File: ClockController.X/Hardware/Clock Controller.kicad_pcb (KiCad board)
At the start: 2 copper layers, 63.5 x 44.5 mm, 48 parts, among them J1 UJC-VP-3-SMT-TR, J2 HDR-1X2H, Q1 DMG7430LFG-7, Q2 FDD7N25LZTM, Q3 MMBT2222A-TP, Q4 MMBT2907ALT1G, Q5 MMBT2222A-TP, Q6 MMBT2222A-TP, U1 PIC16F15224-I/SL, U2 AS78L05RTR-E1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

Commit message: More zones
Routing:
- net +5V: track 51.1 -> 43.0 mm
- added copper zone on B.Cu, net +5V
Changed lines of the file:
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@@
-	)
-	(segment
-		(start 141.985965 119.379965)
-		(end 136.332 119.379965)
-		(width 1.27)
-		(layer "B.Cu")
-		(net 2)
-	)
-	(segment
-		(start 142.24 119.38)
-		(end 141.986 119.38)
-		(width 0.2)
-		(layer "B.Cu")
-		(net 2)
-	)
-	(segment
-		(start 136.332 121.5385)
-		(end 136.27 121.6005)
-		(width 1.27)
-		(layer "B.Cu")
-		(net 2)
-	)
-	(segment
-		(start 136.332 119.379965)
-		(end 136.332 121.5385)
-		(width 1.27)
-		(layer "B.Cu")
-		(net 2)
-	)
-	(segment
-		(start 141.986 119.38)
-		(end 141.985965 119.379965)
-		(width 0.2)
-		(layer "B.Cu")
-		(net 2)
 	)
 	(segment
@@
 	)
 	(zone
+		(net 2)
+		(net_name "+5V")
+		(layer "B.Cu")
+		(hatch edge 0.5)
+		(priority 10)
+		(connect_pads yes
+			(clearance 0.5)
+		)
+		(min_thickness 0.25)
+		(filled_areas_thickness no)
+		(fill yes
+			(thermal_gap 0.5)
+			(thermal_bridge_width 0.5)
+			(smoothing fillet)
+			(radius 0.254)
+		)
+		(polygon
+			(pts
+				(xy 135.89 118.618) (xy 142.494 118.618) (xy 142.494 120.142) (xy 136.906 122.174) (xy 135.636 122.174)
+				(xy 135.636 121.158)
+			)
+		)
+	)
+	(zone

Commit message: Small layout adjustments
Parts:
- moved PWM0 2.30 mm to (141.2, 111.5)
- moved C4 1.65 mm to (166.6, 122.4), turned to 90.0029 degrees
- moved C2 1.50 mm to (134.3, 110.7)
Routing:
- net GND: track 22.7 -> 20.2 mm
- net V5V: track 100.7 -> 98.6 mm

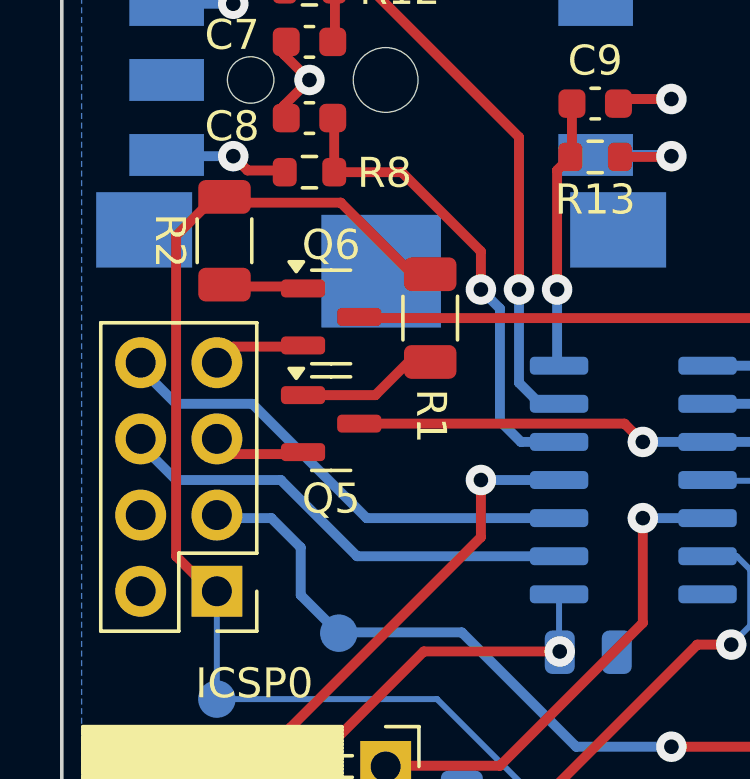
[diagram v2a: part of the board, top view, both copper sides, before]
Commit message: Simplified I2C cutoff
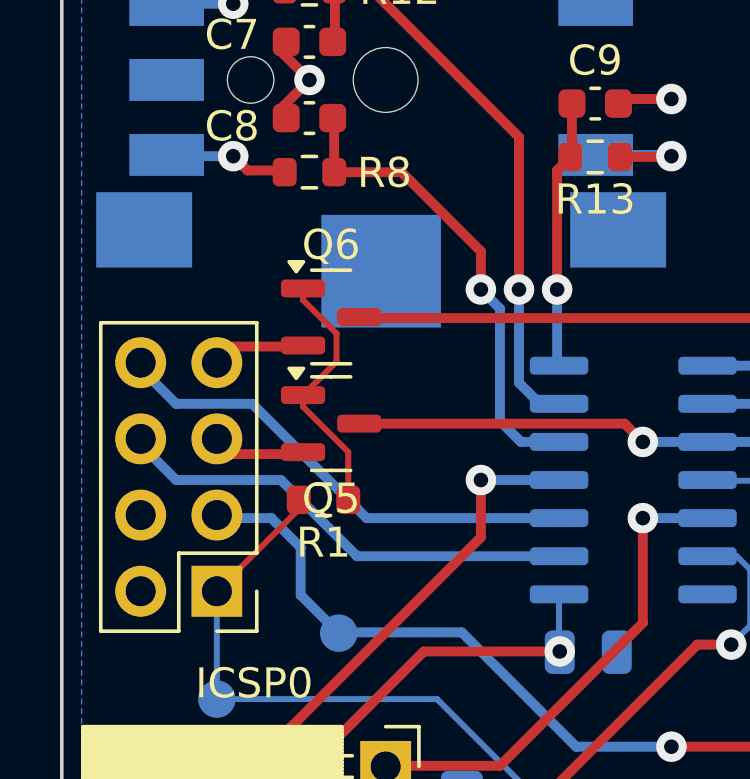
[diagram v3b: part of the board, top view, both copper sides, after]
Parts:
- removed R2: 2.2k, Resistor_SMD:R_1206_3216Metric
- R1: footprint Resistor_SMD:R_1206_3216Metric -> Resistor_SMD:R_0603_1608Metric
- moved R1 7.02 mm to (125.5, 105.7), turned to -179.999 degrees
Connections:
- Q6 pad 1: Net-(Q6-B) -> Net-(Q5-B)
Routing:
- net +5V: track 43.0 -> 25.1 mm
- net Net-(Q5-B): track 4.19 -> 8.60 mm
- net Net-(Q6-B): track 2.67 -> 0.00 mm

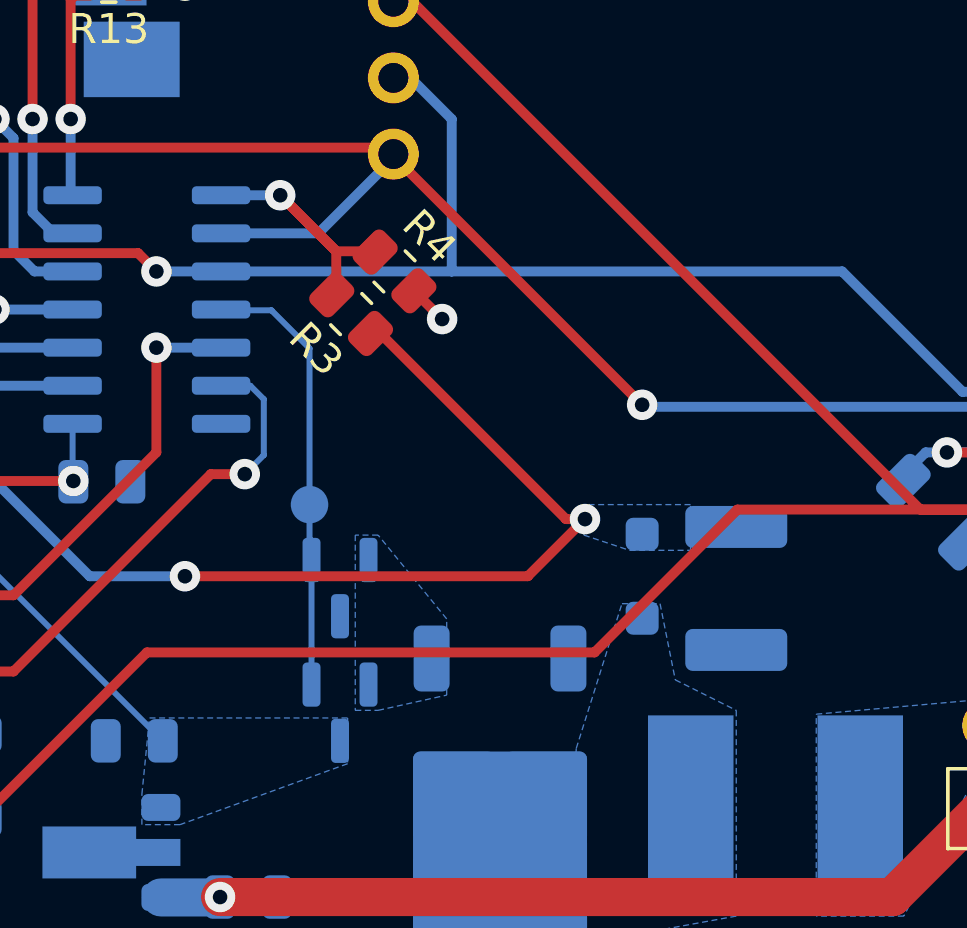
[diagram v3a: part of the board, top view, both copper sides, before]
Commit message: Moved C3
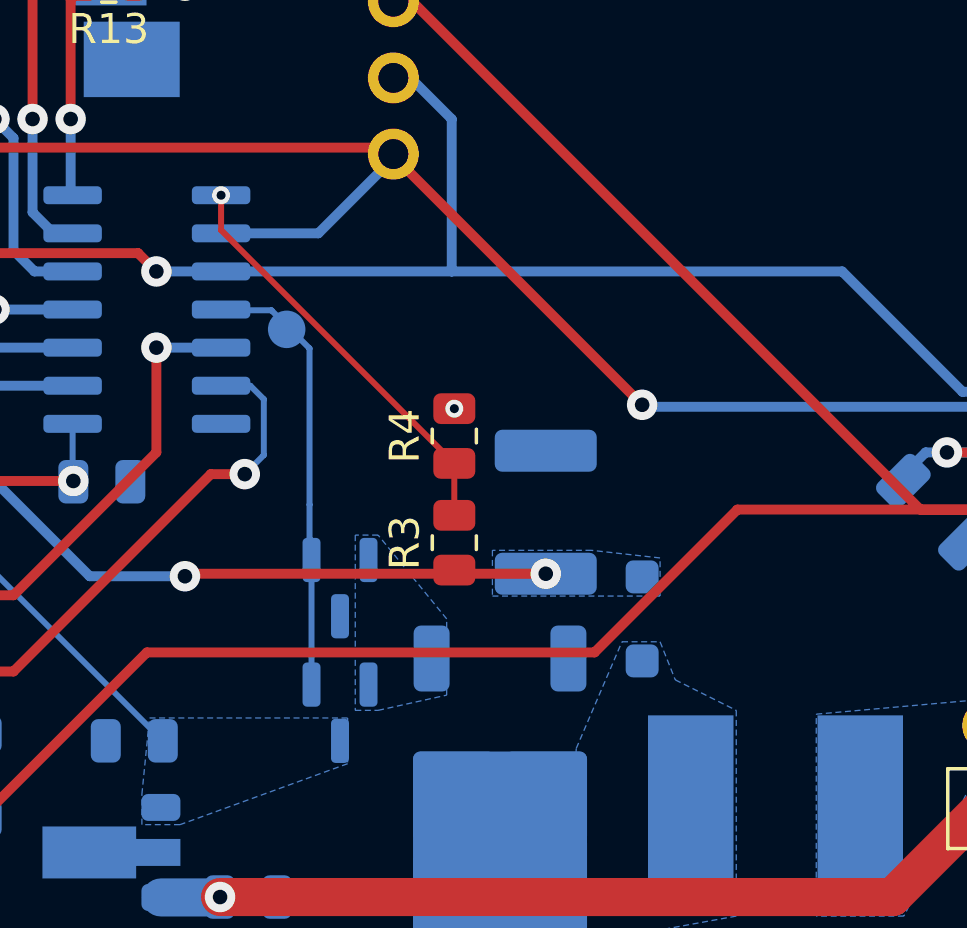
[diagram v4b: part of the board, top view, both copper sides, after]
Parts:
- moved R3 8.36 mm to (146.1, 112.8), turned to 90 degrees
- moved C3 6.84 mm to (149.1, 111.8), turned to -89.9952 degrees
- moved PWM0 5.89 mm to (140.5, 105.7)
- moved R4 5.84 mm to (146.1, 109.2), turned to 90 degrees
- moved D1 1.42 mm to (152.3, 115.3)
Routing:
- net VNN: track 43.0 -> 31.4 mm
- net HV_Mon: track 9.85 -> 13.9 mm
- net GND: track 20.2 -> 18.9 mm
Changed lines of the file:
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@@
 	(footprint "Resistor_SMD:R_0805_2012Metric"
 		(layer "F.Cu")
-		(at 142.610765 105.156 135)
+		(at 146.05 112.776 90)
 		(descr "Resistor SMD 0805 (2012 Metric), square (rectangular) end terminal, IPC_7351 nominal, (Body size source: IPC-SM-782 page 72, https://www.pcb-3d.com/wordpress/wp-content/uploads/ipc-sm-782a_amendment_1_and_2.pdf), generated with kicad-footprint-generator")
 		(tags "resistor")
 		(property "Reference" "R3"
-			(at 0 -1.65 135)
+			(at 0 -1.65 90)
 			(layer "F.SilkS")
 			(effects
@@
 		)
 		(property "Value" "750k"
-			(at 0 1.65 135)
+			(at 0 1.65 90)
 			(layer "F.Fab")
 			(effects
@@
 		)
 		(property "Datasheet" ""
-			(at 0 0 135)
+			(at 0 0 90)
 			(unlocked yes)
 			(layer "F.Fab")
@@
 		)
 		(property "Description" ""
-			(at 0 0 135)
+			(at 0 0 90)
 			(unlocked yes)
 			(layer "F.Fab")
@@
 		)
 		(fp_line
-			(start 1.68 0.95)
-			(end -1.68 0.95)
+			(start -1.68 -0.95)
+			(end 1.68 -0.95)
 			(stroke
 				(width 0.05)
@@
 		)
 		(fp_line
-			(start -1.68 -0.95)
-			(end 1.68 -0.95)
+			(start 1.68 0.95)
+			(end -1.68 0.95)
 			(stroke
 				(width 0.05)
@@
 		)
 		(fp_line
-			(start 1 0.625)
-			(end -1 0.625)
+			(start -1 -0.625)
+			(end 1 -0.625)
 			(stroke
 				(width 0.1)
@@
 		)
 		(fp_line
-			(start -1 -0.625)
-			(end 1 -0.625)
+			(start 1 0.625)
+			(end -1 0.625)
 			(stroke
 				(width 0.1)
@@
 		)
 		(fp_text user "${REFERENCE}"
-			(at 0 0 135)
+			(at 0 0 90)
 			(layer "F.Fab")
 			(effects
@@
 		)
 		(pad "1" smd roundrect
-			(at -0.9125 0 135)
+			(at -0.9125 0 90)
 			(size 1.025 1.4)
 			(layers "F.Cu" "F.Mask" "F.Paste")
@@
 		)
 		(pad "2" smd roundrect
-			(at 0.9125 0 135)
+			(at 0.9125 0 90)
 			(size 1.025 1.4)
 			(layers "F.Cu" "F.Mask" "F.Paste")
@@
 	(footprint "Resistor_SMD:R_0805_2012Metric"
 		(layer "F.Cu")
-		(at 144.0561 103.7336 -45)
+		(at 146.05 109.22 90)
 		(descr "Resistor SMD 0805 (2012 Metric), square (rectangular) end terminal, IPC_7351 nominal, (Body size source: IPC-SM-782 page 72, https://www.pcb-3d.com/wordpress/wp-content/uploads/ipc-sm-782a_amendment_1_and_2.pdf), generated with kicad-footprint-generator")
 		(tags "resistor")
 		(property "Reference" "R4"
-			(at 0 -1.65 315)
+			(at 0 -1.65 90)
 			(layer "F.SilkS")
 			(effects
@@
 		)
 		(property "Value" "12k"
-			(at 0 1.65 315)
+			(at 0 1.65 90)
 			(layer "F.Fab")
 			(effects
@@
 		)
 		(property "Datasheet" ""
-			(at 0 0 315)
+			(at 0 0 90)
 			(unlocked yes)
 			(layer "F.Fab")
@@
 		)
 		(property "Description" ""
-			(at 0 0 315)
+			(at 0 0 90)
 			(unlocked yes)
 			(layer "F.Fab")
@@
 		(attr smd)
 		(fp_line
-			(start -0.227064 0.735)
-			(end 0.227064 0.735)
+			(start -0.227064 -0.735)
+			(end 0.227064 -0.735)
 			(stroke
 				(width 0.12)
@@
 		)
 		(fp_line
-			(start -0.227064 -0.735)
-			(end 0.227064 -0.735)
+			(start -0.227064 0.735)
+			(end 0.227064 0.735)
 			(stroke
 				(width 0.12)
@@
 		)
 		(fp_line
-			(start -1.68 0.95)
-			(end -1.68 -0.95)
+			(start 1.68 -0.95)
+			(end 1.68 0.95)
 			(stroke
 				(width 0.05)
@@
 		)
 		(fp_line
-			(start 1.68 -0.95)
-			(end 1.68 0.95)
+			(start -1.68 0.95)
+			(end -1.68 -0.95)
 			(stroke
 				(width 0.05)
@@
 		)
 		(fp_line
-			(start -1 0.625)
-			(end -1 -0.625)
+			(start 1 -0.625)
+			(end 1 0.625)
 			(stroke
 				(width 0.1)
@@
 		)
 		(fp_line
-			(start 1 -0.625)
-			(end 1 0.625)
+			(start -1 0.625)
+			(end -1 -0.625)
 			(stroke
 				(width 0.1)
@@
 		)
 		(fp_text user "${REFERENCE}"
-			(at 0 0 315)
+			(at 0 0 90)
 			(layer "F.Fab")
 			(effects
@@
 		)
 		(pad "1" smd roundrect
-			(at -0.9125 0 315)
+			(at -0.9125 0 90)
 			(size 1.025 1.4)
 			(layers "F.Cu" "F.Mask" "F.Paste")
@@
 		)
 		(pad "2" smd roundrect
-			(at 0.9125 0 315)
+			(at 0.9125 0 90)
 			(size 1.025 1.4)
 			(layers "F.Cu" "F.Mask" "F.Paste")
@@
 	(footprint "Diode_SMD:D_SOD-123F"
 		(layer "B.Cu")
-		(at 152.311111 113.8936 -89.99726403)
+		(at 152.311111 115.316 -89.99726403)
 		(descr "D_SOD-123F")
 		(tags "D_SOD-123F")
 		(property "Reference" "D1"
-			(at -0.127 1.905 90.00273597)
+			(at 0.000089 -1.866889 90.00273597)
 			(layer "B.SilkS")
 			(effects
@@
 	(footprint "Clock Controller:TP_1.25MM"
 		(layer "B.Cu")
-		(at 141.224 111.506 90.002)
+		(at 140.462 105.664 90.002)
 		(property "Reference" "PWM0"
 			(at 0 0 90.002)
@@
 	(footprint "Capacitor_SMD:C_1812_4532Metric"
 		(layer "B.Cu")
-		(at 155.448 114.3 90.00484056)
+		(at 149.098 111.76 -89.99515944)
 		(descr "Capacitor SMD 1812 (4532 Metric), square (rectangular) end terminal, IPC-7351 nominal, (Body size source: IPC-SM-782 page 76, https://www.pcb-3d.com/wordpress/wp-content/uploads/ipc-sm-782a_amendment_1_and_2.pdf), generated with kicad-footprint-generator")
 		(tags "capacitor")
 		(property "Reference" "C3"
-			(at 0 2.65 270.0048406)
+			(at -3.81 -0.000322 180.0048406)
 			(layer "B.SilkS")
 			(effects
@@
 		)
 		(property "Value" "10uF"
-			(at 0 -2.65 270.0048406)
+			(at 0 -2.65 90.0048406)
 			(layer "B.Fab")
 			(effects
@@
 		)
 		(property "Datasheet" ""
-			(at 0 0 270.0048406)
+			(at 0 0 90.0048406)
 			(layer "B.Fab")
 			(hide yes)
@@
 		)
 		(property "Description" ""
-			(at 0 0 270.0048406)
+			(at 0 0 90.0048406)
 			(layer "B.Fab")
 			(hide yes)
@@
 		(attr smd)
 		(fp_line
-			(start -1.161252 -1.71)
-			(end 1.161252 -1.71)
+			(start -1.161252 1.71)
+			(end 1.161252 1.71)
 			(stroke
 				(width 0.12)
@@
 		)
 		(fp_line
-			(start -1.161252 1.71)
-			(end 1.161252 1.71)
+			(start -1.161252 -1.71)
+			(end 1.161252 -1.71)
 			(stroke
 				(width 0.12)
@@
 		)
 		(fp_text user "${REFERENCE}"
-			(at 0 0 270.0048406)
+			(at 0 0 90.0048406)
 			(layer "B.Fab")
 			(effects
@@
 		)
 		(pad "1" smd roundrect
-			(at -2.05 0 90.00484056)
+			(at -2.05 0 270.0048406)
 			(size 1.4 3.4)
 			(layers "B.Cu" "B.Mask" "B.Paste")
@@
 		)
 		(pad "2" smd roundrect
-			(at 2.05 0 90.00484056)
+			(at 2.05 0 270.0048406)
 			(size 1.4 3.4)
 			(layers "B.Cu" "B.Mask" "B.Paste")
@@
 	)
 	(gr_text "PWM"
-		(at 146.558 112.268 359.9976849)
+		(at 145.796 106.426 359.9976849)
 		(layer "B.SilkS")
 		(effects
@@
 	)
 	(segment
-		(start 144.727867 104.405367)
-		(end 144.727867 104.405367)
-		(width 0.33)
-		(layer "F.Cu")
-		(net 8)
-	)
-	(segment
 		(start 124.1561 92.938633)
 		(end 124.1561 92.5186)
@@
 	)
 	(segment
-		(start 145.6436 105.3211)
-		(end 144.727867 104.405367)
-		(width 0.33)
-		(layer "F.Cu")
-		(net 8)
-	)
-	(segment
 		(start 124.1561 92.5186)
 		(end 125.0061 91.6686)
@@
 	)
 	(via
-		(at 165.6461 105.3211)
-		(size 1.016)
-		(drill 0.485667)
+		(at 146.05 108.3075)
+		(size 0.6)
+		(drill 0.3)
 		(layers "F.Cu" "B.Cu")
 		(net 8)
 	)
 	(via
-		(at 145.6436 105.3211)
+		(at 165.6461 105.3211)
 		(size 1.016)
 		(drill 0.485667)
@@
 	)
 	(segment
-		(start 140.2461 101.1936)
-		(end 142.114333 103.061833)
-		(width 0.33)
-		(layer "F.Cu")
-		(net 9)
-	)
-	(segment
-		(start 140.2461 101.1936)
-		(end 142.114333 103.061833)
-		(width 0.33)
+		(start 146.05 111.8635)
+		(end 146.05 110.1325)
+		(width 0.2)
 		(layer "F.Cu")
 		(net 9)
 	)
 	(segment
-		(start 142.114333 103.061833)
-		(end 142.114333 104.331833)
-		(width 0.33)
+		(start 138.2761 102.3586)
+		(end 138.2761 101.1936)
+		(width 0.2)
 		(layer "F.Cu")
 		(net 9)
 	)
 	(segment
-		(start 142.114333 103.061833)
-		(end 143.384333 103.061833)
-		(width 0.33)
+		(start 146.05 110.1325)
+		(end 138.2761 102.3586)
+		(width 0.2)
 		(layer "F.Cu")
 		(net 9)
 	)
 	(via
-		(at 140.2461 101.1936)
-		(size 1.016)
-		(drill 0.485667)
+		(at 138.2761 101.1936)
+		(size 0.6)
+		(drill 0.3)
 		(layers "F.Cu" "B.Cu")
 		(net 9)
 	)
 	(segment
-		(start 140.2461 101.1936)
-		(end 140.2461 101.1936)
-		(width 0.33)
-		(layer "B.Cu")
-		(net 9)
-	)
-	(segment
-		(start 138.2211 101.1936)
-		(end 140.2461 101.1936)
-		(width 0.33)
-		(layer "B.Cu")
-		(net 9)
-	)
-	(segment
 		(start 163.7561 104.1636)
 		(end 164.1861 103.7336)
@@
 	)
 	(segment
-		(start 148.5011 113.8936)
-		(end 150.4061 111.9886)
+		(start 137.1547 113.81)
+		(end 149.098173 113.81)
 		(width 0.33)
 		(layer "F.Cu")
@@
 	(segment
 		(start 137.0711 113.8936)
-		(end 148.5011 113.8936)
-		(width 0.33)
-		(layer "F.Cu")
-		(net 19)
-	)
-	(segment
-		(start 143.457867 105.675367)
-		(end 149.7711 111.9886)
-		(width 0.33)
-		(layer "F.Cu")
-		(net 19)
-	)
-	(segment
-		(start 149.7711 111.9886)
-		(end 150.4061 111.9886)
+		(end 137.1547 113.81)
 		(width 0.33)
 		(layer "F.Cu")
@@
 	)
 	(via
-		(at 150.4061 111.9886)
+		(at 149.098173 113.81)
 		(size 1.016)
 		(drill 0.485667)
@@
 		(polygon
 			(pts
-				(xy 150.368 111.506) (xy 150.368 112.522) (xy 151.892 113.03) (xy 153.924 113.03) (xy 153.924 111.506)
+				(xy 147.32 113.03) (xy 147.32 114.554) (xy 152.908 114.554) (xy 152.908 113.284) (xy 150.622 113.03)
 			)
 		)
@@
 		(polygon
 			(pts
-				(xy 152.908 114.808) (xy 153.416 117.348) (xy 155.448 118.364) (xy 155.448 125.222) (xy 149.86 126.238)
-				(xy 150.114 119.634) (xy 151.638 114.808)
+				(xy 152.908 116.078) (xy 153.416 117.348) (xy 155.448 118.364) (xy 155.448 125.222) (xy 149.86 126.238)
+				(xy 150.114 119.634) (xy 151.638 116.078)
 			)
 		)
